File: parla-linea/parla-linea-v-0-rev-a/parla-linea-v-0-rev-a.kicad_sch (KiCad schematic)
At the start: 0 parts

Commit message: agregar mas apuntes
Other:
- company: (none) -> piruetas SpA
- title: (none) -> parla-linea-v-0
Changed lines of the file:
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@@
 (kicad_sch
-  (version 20260306)
-  (generator "eeschema")
-  (generator_version "10.0")
-  (paper "A4")
-  (sheet_instances
-    (path "/"
-      (page "1")))
-  (embedded_fonts no))
+	(version 20260306)
+	(generator "eeschema")
+	(generator_version "10.0")
+	(paper "A4")
+	(title_block
+		(title "parla-linea-v-0")
+		(date "2026-10-01")
+		(rev "rev-a")
+		(company "piruetas SpA")
+	)
+	(sheet_instances
+		(path "/"
+			(page "1")
+		)
+	)
+	(embedded_fonts no)
+)

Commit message: nueva version de parla linea
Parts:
- added C1: C_Polarized, symbol Device:C_Polarized
- added C2, C5: 100n, symbol Device:C
- added C3: 100u, symbol Device:C_Polarized
- added C4: 10u, symbol Device:C_Polarized
- added D1: 1N4007, symbol Device:D
- added D2: LED, symbol Device:LED
- added J1: AudioJack3_SwitchT, symbol Connector_Audio:AudioJack3_SwitchT
- added J2: AudioJack2_SwitchT, symbol Connector_Audio:AudioJack2_SwitchT
- added J3: Screw_Terminal_01x02, symbol Connector:Screw_Terminal_01x02
- added R1, R2: 10k, symbol Device:R
- added R3: 1k, symbol Device:R
- added RV1: A10k, symbol Device:R_Potentiometer
- added U1: PAM8403D, Package_SO:SOIC-16_3.9x9.9mm_P1.27mm, symbol Amplifier_Audio:PAM8403D
- added U2: L7805, symbol Regulator_Linear:L7805
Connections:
- new net: D2.1 (K), R3.1
- new net: C2.1, U1.8 (VREF)
- new net: C1.1, R1.2, R2.2
- new net: C1.2, RV1.1
- new net: J1.R, R2.1
- new net: J1.T, R1.1
- new net: C3.1, D1.1 (K), U2.1 (IN)
- new net: J2.3, U1.1 (LOUT+)
- new net: J2.1, U1.3 (LOUT-)
- new net: RV1.2, U1.7 (INL)
- new net +5V: C4.1, C5.1, D2.2 (A), U1.13 (PVDD), U1.4 (PVDD), U1.6 (VDD), U2.3 (OUT)
- new net +9V: D1.2 (A), J3.1 (Pin_1)
- new net GND: C2.2, C3.2, C4.2, C5.2, J1.S, J3.2 (Pin_2), R3.2, RV1.3, U1.10 (INR), U1.11 (GND), U1.15 (PGND), U1.2 (PGND), U2.2 (GND)
- no-connect marks 0 -> 6
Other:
- note added: "entrada jack TRS stereo se suman left y right"
- note added: "salida mono a un parlante"
- note added: "tip - left ring - right sleeve - ground"

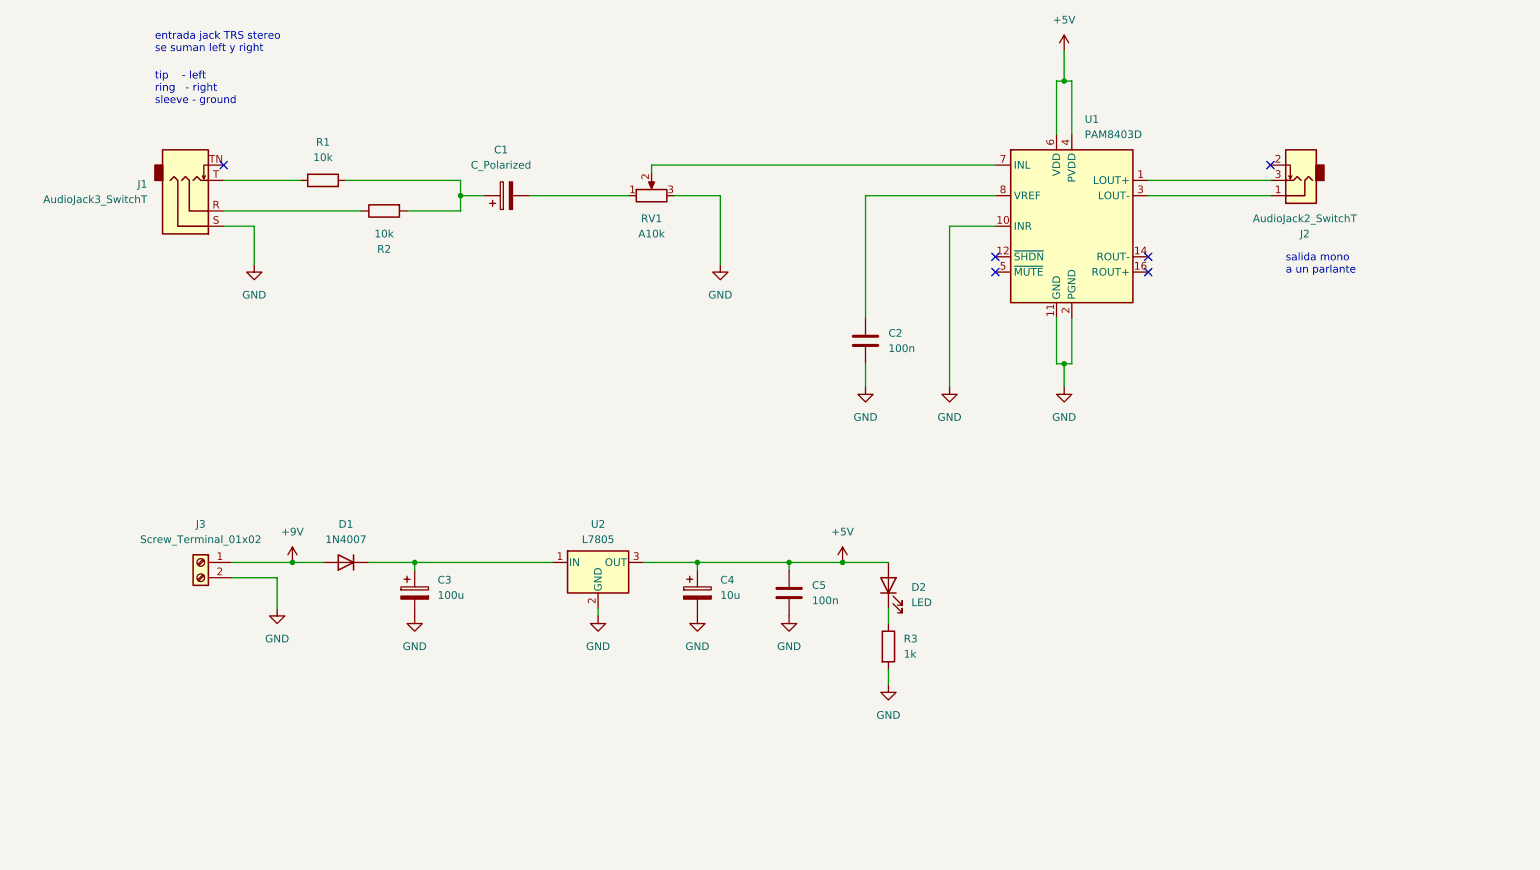
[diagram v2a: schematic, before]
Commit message: agregar mas sobre parla linea extensor
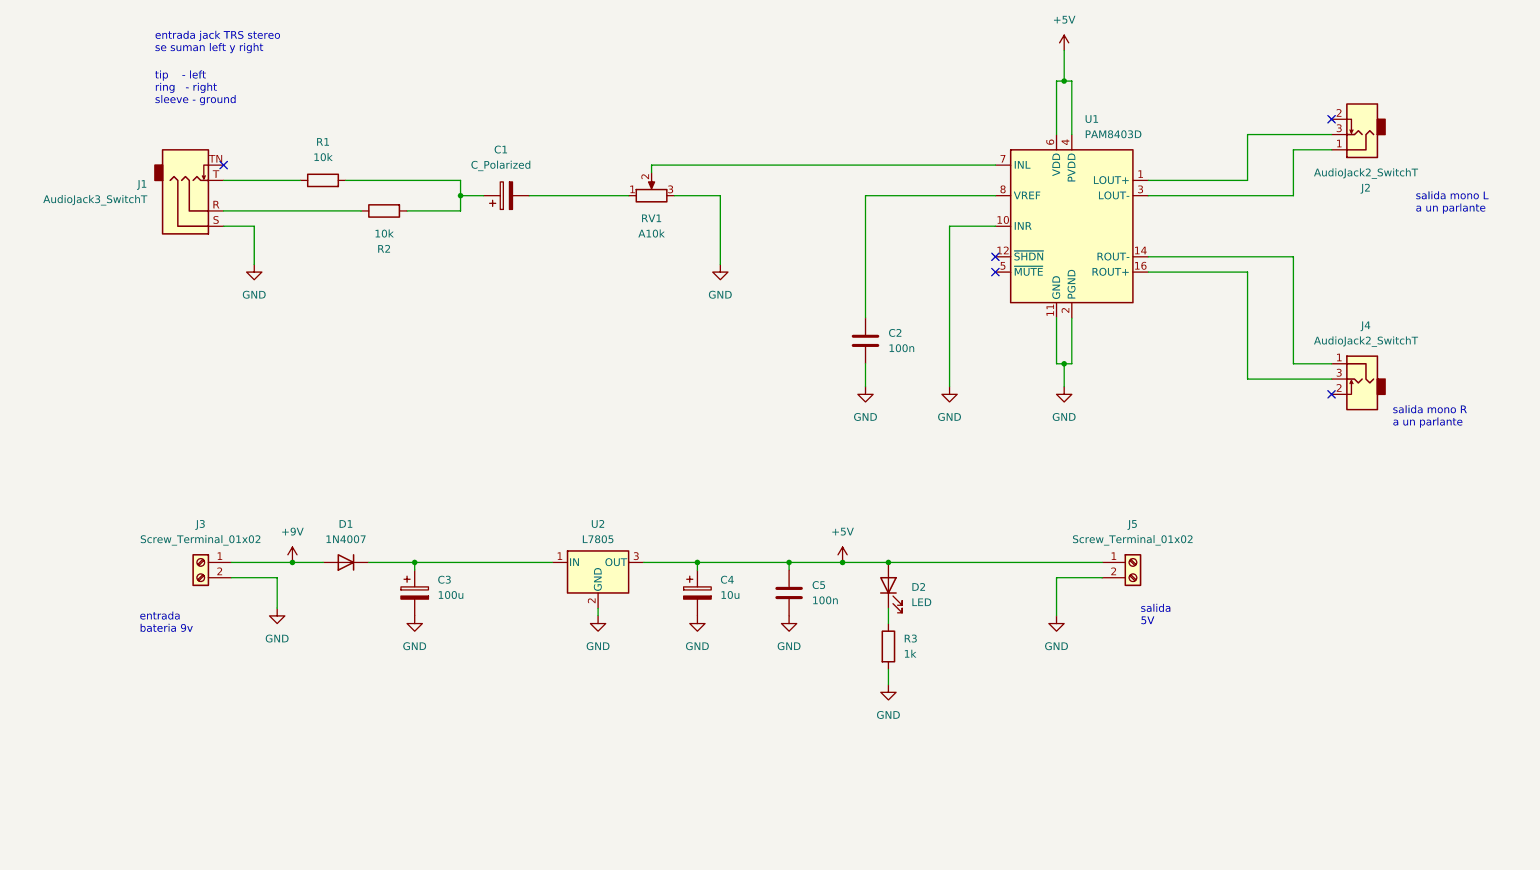
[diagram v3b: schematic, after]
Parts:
- added J4: AudioJack2_SwitchT, symbol Connector_Audio:AudioJack2_SwitchT
- added J5: Screw_Terminal_01x02, symbol Connector:Screw_Terminal_01x02
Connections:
- net +5V: now also J5.1 (Pin_1)
- net GND: now also J5.2 (Pin_2)
- net at U1.14 (ROUT-): now also J4.1
- net at U1.16 (ROUT+): now also J4.3
- no-connect marks 6 -> 5
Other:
- note added: "entrada bateria 9v"
- note added: "salida 5V"
- note added: "salida mono L a un parlante"
- note added: "salida mono R a un parlante"
- note removed: "salida mono a un parlante"
- moved on the sheet: J2

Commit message: añadidos componentes lcsc
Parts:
- removed C1: C_Polarized, symbol Device:C_Polarized
- removed C5: 100n, symbol Device:C
- removed J1: AudioJack3_SwitchT, symbol Connector_Audio:AudioJack3_SwitchT
- removed RV1: A10k, symbol Device:R_Potentiometer
- added C1, C6: C, symbol Device:C
- added C7: 100n, symbol Device:C
- added J6: AudioJack3_SwitchTR, Connector_Audio:Jack_3.5mm_CUI_SJ1-3525N_Horizontal, symbol Connector_Audio:AudioJack3_SwitchTR
- added J7: Conn_01x03_Pin, Connector_PinHeader_2.54mm:PinHeader_1x03_P2.54mm_Vertical, symbol Connector:Conn_01x03_Pin
- added RV1: 100kB, Potentiometer_THT:Potentiometer_Alps_RK163_Dual_Horizontal, symbol Device:R_Potentiometer_Dual_Separate
- C2: LCSC (none) -> C49678
- C3: LCSC (none) -> C72478
- C4: LCSC (none) -> C72485
- D1: LCSC (none) -> C193404
- D2: footprint (none) -> Eurocad:LED3mm
- J2, J4: footprint (none) -> Connector_Audio:Jack_3.5mm_QingPu_WQP-PJ398SM_Vertical_CircularHoles
- J3, J5: footprint (none) -> TerminalBlock:TerminalBlock_MaiXu_MX126-5.0-02P_1x02_P5.00mm
- R1, R2: LCSC (none) -> C17414
- R3: LCSC (none) -> C2907232
- U1: LCSC (none) -> C5122557
- U2: LCSC (none) -> C19626525
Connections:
- net +5V: now also C7.1
- net GND: now also C7.2, J6.S, RV1.1, RV1.4; no longer U1.10 (INR)
- net at R1.2: now also C1.1, J7.3 (Pin_3); no longer R2.2
- net at R2.1: now also J7.2 (Pin_2)
- net at R1.1: now also J6.T, J6.TN
- net at U1.7 (INL): now also RV1.2
- new net: C6.1, J7.1 (Pin_1)
- new net: C1.2, RV1.3
- new net: RV1.5, U1.10 (INR)
- new net: C6.2, RV1.6
- new net: J6.R, J6.RN, R2.2
- no-connect marks 5 -> 4
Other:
- note added: "puenteando 1 y 2 -> L R separado puenteando 2 y 3 -> suma L + R sin puente -> solo L pasa"
- note added: "puenteando 5 y 4 en el pot se puede tirar IN R a GND"
- note removed: "entrada jack TRS stereo se suman left y right"
- moved on the sheet: C2, C3, C4, D1, D2, J3, J5, R3, U2

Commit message: trazado
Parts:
- removed J4: AudioJack2_SwitchT, Connector_Audio:Jack_3.5mm_QingPu_WQP-PJ398SM_Vertical_CircularHoles, symbol Connector_Audio:AudioJack2_SwitchT
- added H1, H2, H3, H4: M3, MountingHole:MountingHole_3.2mm_M3, symbol Mechanical:MountingHole
- added J1: AudioJack2_SwitchT, Connector_Audio:Jack_3.5mm_QingPu_WQP-PJ398SM_Vertical_CircularHoles, symbol Connector_Audio:AudioJack2_SwitchT
- added J4: Conn_01x01, Connector_Wire:SolderWire-0.25sqmm_1x01_D0.65mm_OD1.7mm, symbol Connector_Generic:Conn_01x01
- C1, C2, C6, C7: footprint (none) -> parla-linea-v-0-rev-a:C0805
- C3: footprint (none) -> parla-linea-v-0-rev-a:CAP-SMD_BD6.3-L6.6-W6.6-LS7.6-FD
- C4: footprint (none) -> parla-linea-v-0-rev-a:CAP-SMD_BD4.0-L4.3-W4.3-FD
- D1: footprint (none) -> parla-linea-v-0-rev-a:SOD-323_L1.8-W1.3-LS2.5-RD
- R1, R2, R3: footprint (none) -> parla-linea-v-0-rev-a:R0805
- U1: footprint Package_SO:SOIC-16_3.9x9.9mm_P1.27mm -> parla-linea-v-0-rev-a:SOP-16_L10.0-W3.9-P1.27-LS6.0-BL
- U2: footprint (none) -> parla-linea-v-0-rev-a:TO-252-2_L6.6-W6.1-P4.57-LS9.9-BR-CW
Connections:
- net GND: now also J4.1 (Pin_1)
- net at U1.14 (ROUT-): now also J2.S
- net at U1.16 (ROUT+): now also J2.T
- net at U1.1 (LOUT+): now also J1.T; no longer J2.3
- net at U1.3 (LOUT-): now also J1.S; no longer J2.1
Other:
- note added: "salida o entrada 5v"
- note removed: "salida 5V"

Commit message: agregar pcba
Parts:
- C1, C6: value C -> 1u
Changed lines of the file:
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@@
 			)
 		)
-		(property "Value" "C"
+		(property "Value" "1u"
 			(at 94.996 91.44 90)
 			(show_name no)
@@
 			)
 		)
-		(property "Value" "C"
+		(property "Value" "1u"
 			(at 95.25 63.5 90)
 			(show_name no)
